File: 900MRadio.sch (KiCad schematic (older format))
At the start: 0 parts

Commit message: Added more RF components
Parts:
- added U3: CC1120, SMD_Packages:RHB_S-PVQFN-N32, symbol CC1120
- added U4: CC1190, SMD_Packages:RGV_S-PVQFN-N16, symbol CC1190
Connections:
- new net GND: U3.EP (GND), U4.1 (GND), U4.12 (GND), U4.3 (GND), U4.9 (GND), U4.EP (GND)
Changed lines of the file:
@@
 $Descr A4 11693 8268
 encoding utf-8
-Sheet 1 3
+Sheet 3 3
 Title ""
 Date ""
@@
 Comment4 ""
 $EndDescr
+$Comp
+L CC1120 U3
+U 1 1 559BFDEE
+P 2900 3850
+F 0 "U3" H 2400 2800 60  0000 C CNN
+F 1 "CC1120" H 3250 2800 60  0000 C CNN
+F 2 "SMD_Packages:RHB_S-PVQFN-N32" H 2900 3850 60  0001 C CNN
+F 3 "" H 2900 3850 60  0000 C CNN
+	1    2900 3850
+	1    0    0    -1
+$EndComp
+$Comp
+L GND #PWR021
+U 1 1 559BFF7D
+P 2900 5000
+F 0 "#PWR021" H 2900 4750 50  0001 C CNN
+F 1 "GND" H 2900 4850 50  0000 C CNN
+F 2 "" H 2900 5000 60  0000 C CNN
+F 3 "" H 2900 5000 60  0000 C CNN
+	1    2900 5000
+	1    0    0    -1
+$EndComp
+$Comp
+L CC1190 U4
+U 1 1 559C0282
+P 7050 4250
+F 0 "U4" H 6600 3700 60  0000 C CNN
+F 1 "CC1190" H 6700 4800 60  0000 C CNN
+F 2 "SMD_Packages:RGV_S-PVQFN-N16" H 7050 4250 60  0001 C CNN
+F 3 "" H 7050 4250 60  0000 C CNN
+	1    7050 4250
+	1    0    0    -1
+$EndComp
+$Comp
+L GND #PWR022
+U 1 1 559C0581
+P 7050 4900
+F 0 "#PWR022" H 7050 4650 50  0001 C CNN
+F 1 "GND" H 7050 4750 50  0000 C CNN
+F 2 "" H 7050 4900 60  0000 C CNN
+F 3 "" H 7050 4900 60  0000 C CNN
+	1    7050 4900
+	1    0    0    -1
+$EndComp
 $EndSCHEMATC

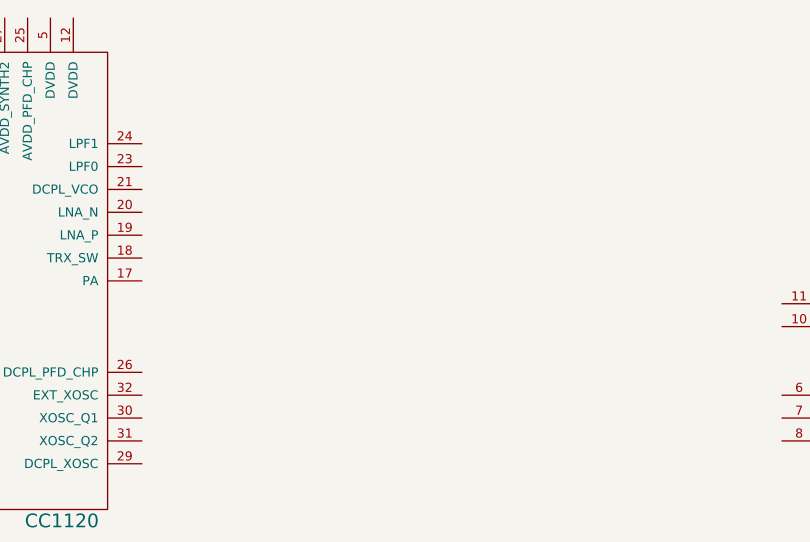
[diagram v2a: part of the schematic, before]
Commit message: Added baluns
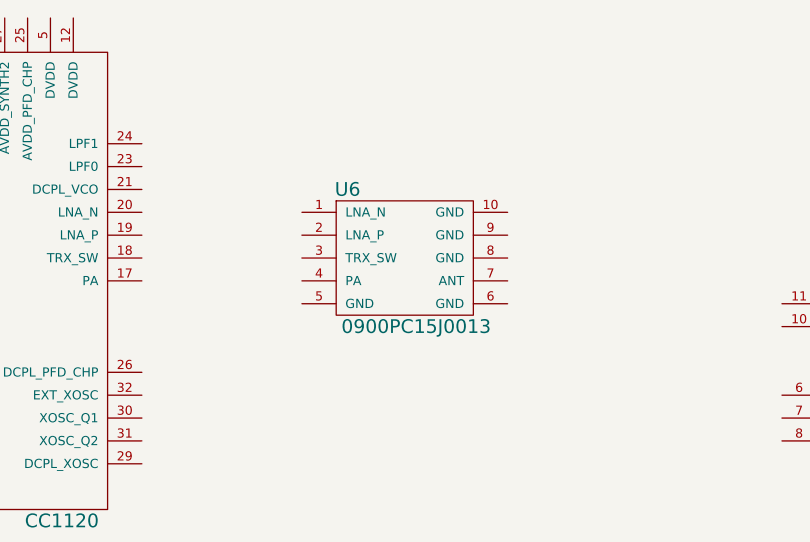
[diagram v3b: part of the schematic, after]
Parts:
- added U6: 0900PC15J0013, SMD_Packages:0900PC15J0013, symbol 0900PC15J0013
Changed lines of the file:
@@
+	1    0    0    -1
+$EndComp
+$Comp
+L 0900PC15J0013 U6
+U 1 1 559C9B74
+P 4750 3750
+F 0 "U6" H 4500 4050 60  0000 C CNN
+F 1 "0900PC15J0013" H 4800 3450 60  0000 C CNN
+F 2 "SMD_Packages:0900PC15J0013" H 4750 3750 60  0001 C CNN
+F 3 "" H 4750 3750 60  0000 C CNN
+	1    4750 3750
 	1    0    0    -1
 $EndComp

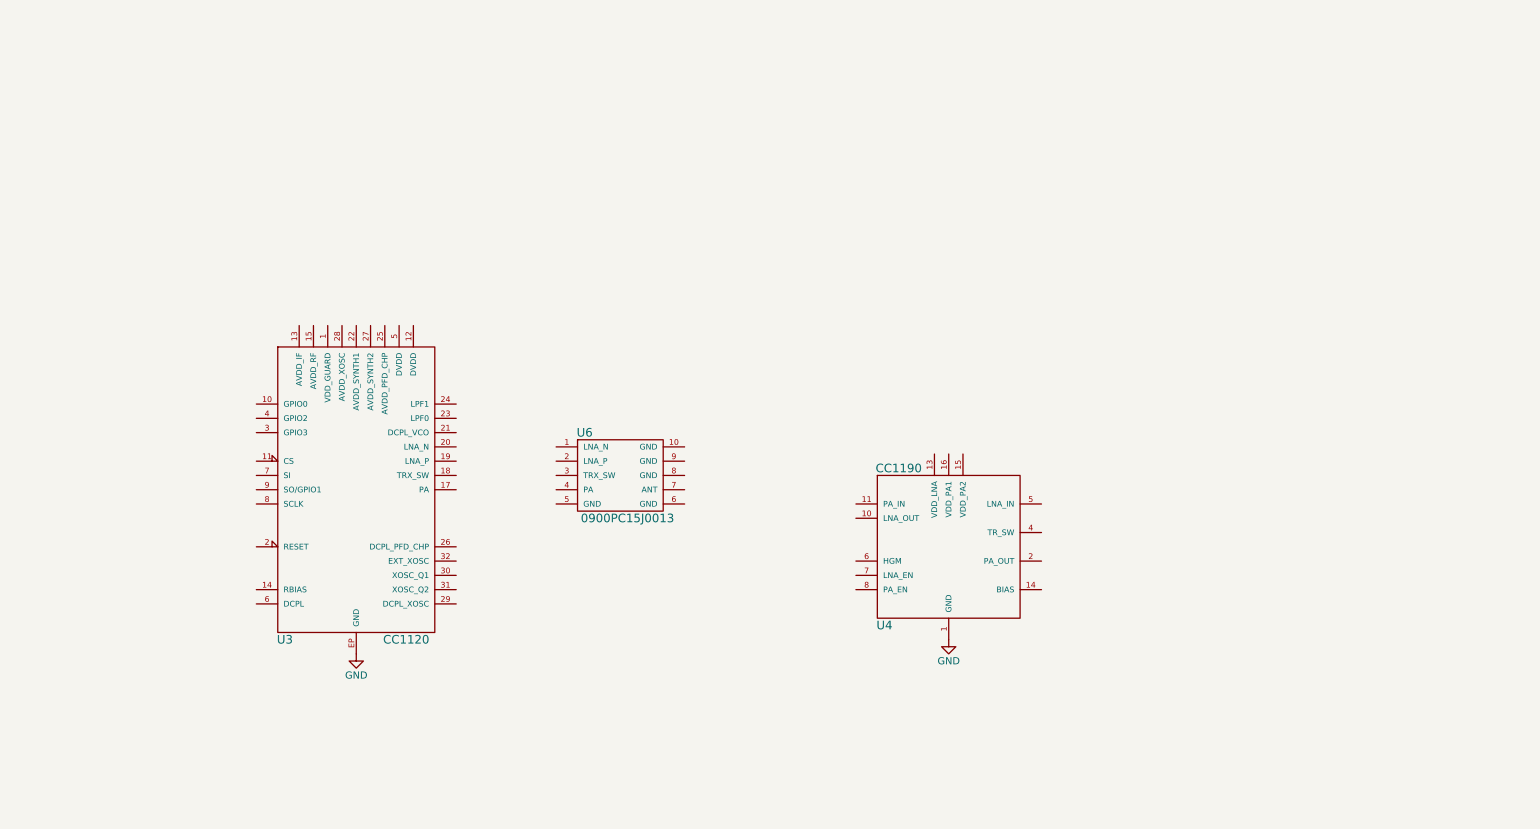
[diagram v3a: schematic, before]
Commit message: Finished schematic of 2.4GHz and 900MHz radios
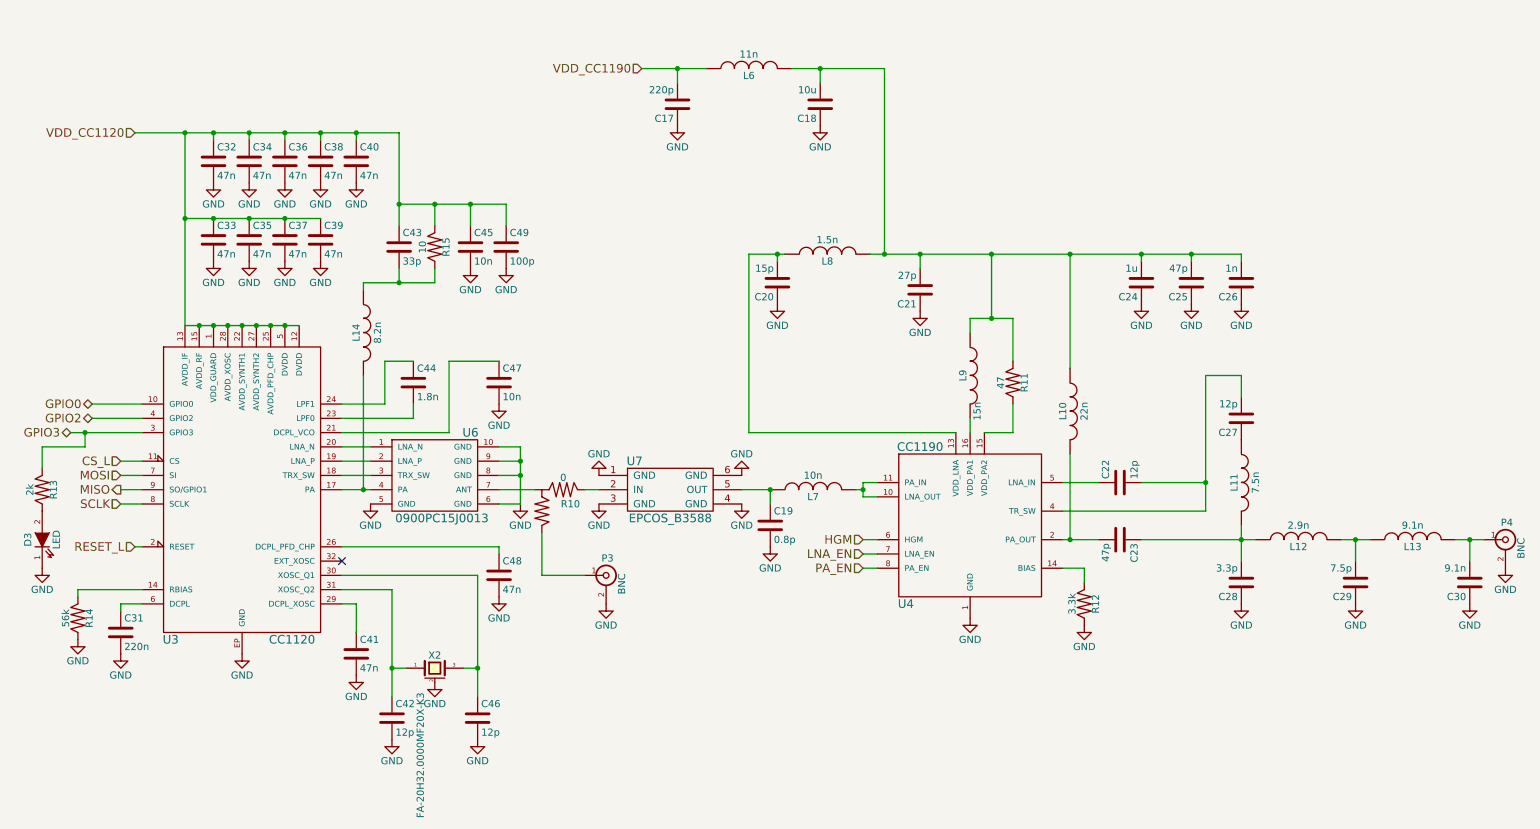
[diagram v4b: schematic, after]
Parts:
- added C17: 220p, Capacitors_SMD:C_0402, symbol C
- added C18: 10u, Capacitors_SMD:C_0402, symbol C
- added C19: 0.8p, Capacitors_SMD:C_0402, symbol C
- added C20: 15p, Capacitors_SMD:C_0402, symbol C
- added C21: 27p, Capacitors_SMD:C_0402, symbol C
- added C22, C27, C42, C46: 12p, Capacitors_SMD:C_0402, symbol C
- added C23, C25: 47p, Capacitors_SMD:C_0402, symbol C
- added C24: 1u, Capacitors_SMD:C_0402, symbol C
- added C26: 1n, Capacitors_SMD:C_0402, symbol C
- added C28: 3.3p, Capacitors_SMD:C_0402, symbol C
- added C29: 7.5p, Capacitors_SMD:C_0402, symbol C
- added C30: 9.1n, Capacitors_SMD:C_0402, symbol C
- added C31: 220n, Capacitors_SMD:C_0402, symbol C
- added C32, C33, C34, C35, C36, C37, C38, C39, C40, C41, C48: 47n, Capacitors_SMD:C_0402, symbol C
- added C43: 33p, Capacitors_SMD:C_0402, symbol C
- added C44: 1.8n, Capacitors_SMD:C_0402, symbol C
- added C45, C47: 10n, Capacitors_SMD:C_0402, symbol C
- added C49: 100p, Capacitors_SMD:C_0402, symbol C
- added D3: LED, LEDs:LED-0603, symbol LED
- added L10: 22n, Resistors_SMD:R_0402, symbol INDUCTOR
- added L11: 7.5n, Resistors_SMD:R_0402, symbol INDUCTOR
- added L12: 2.9n, Resistors_SMD:R_0402, symbol INDUCTOR
- added L13: 9.1n, Resistors_SMD:R_0402, symbol INDUCTOR
- added L14: 8.2n, Resistors_SMD:R_0402, symbol INDUCTOR
- added L6: 11n, Resistors_SMD:R_0402, symbol INDUCTOR
- added L7: 10n, Resistors_SMD:R_0402, symbol INDUCTOR
- added L8: 1.5n, Resistors_SMD:R_0402, symbol INDUCTOR
- added L9: 15n, Resistors_SMD:R_0402, symbol INDUCTOR
- added P3, P4: BNC, Connect:SMB_Straight, symbol BNC
- added R10: 0, Resistors_SMD:R3_LH_0402, symbol R3-LH
- added R11: 47, Resistors_SMD:R_0402, symbol R
- added R12: 3.3k, Resistors_SMD:R_0402, symbol R
- added R13: 2k, Resistors_SMD:R_0402, symbol R
- added R14: 56k, Resistors_SMD:R_0402, symbol R
- added R15: 10, Resistors_SMD:R_0402, symbol R
- added U7: EPCOS_B3588, SMD_Packages:DCC6C, symbol EPCOS_B3588
- added X2: FA-20H32.0000MF20X-K3, Crystals_Oscillators_SMD:FA-20H, symbol CRYSTAL_SMD
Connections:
- net GND: now also U6.10 (GND), U6.5 (GND), U6.6 (GND), U6.8 (GND), U6.9 (GND), C17.1, C18.1, C19.2, C20.1, C21.1, C24.1, C25.1, C26.1, C28.1, C29.1, C30.1, C31.2, C32.2, C33.2, C34.2, C35.2, C36.2, C37.2, C38.2, C39.2, C40.2, C41.2, C42.2, C45.2, C46.2, C47.2, C48.2, C49.2, D3.1 (K), P3.2 (Ext), P4.2 (Ext), R12.2, R14.2, U7.1 (GND), U7.3 (GND), U7.4 (GND), U7.6 (GND), X2.2 (gnd), X2.4 (gnd)
- net VDD_CC1120: now reaches U3.1 (VDD_GUARD)
- net VDD_CC1120: now also U3.12 (DVDD), U3.13 (AVDD_IF), U3.15 (AVDD_RF), U3.22 (AVDD_SYNTH1), U3.25 (AVDD_PFD_CHP), U3.27 (AVDD_SYNTH2), U3.28 (AVDD_XOSC), U3.5 (DVDD), C32.1, C33.1, C34.1, C35.1, C36.1, C37.1, C38.1, C39.1, C40.1, C43.1, C45.1, C49.1, R15.1
- net GPIO0: now reaches U3.10 (GPIO0)
- net CS_L: now reaches U3.11 (CS)
- net at U3.14 (RBIAS): now also R14.1
- net at U3.17 (PA): now also U6.4 (PA), L14.2
- net at U3.18 (TRX_SW): now also U6.3 (TRX_SW)
- net at U3.19 (LNA_P): now also U6.2 (LNA_P)
- net RESET_L: now reaches U3.2 (RESET)
- net at U3.20 (LNA_N): now also U6.1 (LNA_N)
- net at U3.21 (DCPL_VCO): now also C47.1
- net at U3.23 (LPF0): now also C44.2
- net at U3.24 (LPF1): now also C44.1
- net at U3.26 (DCPL_PFD_CHP): now also C48.1
- net at U3.29 (DCPL_XOSC): now also C41.1
- net GPIO3: now reaches U3.3 (GPIO3)
- net GPIO3: now also R13.1
- net at U3.30 (XOSC_Q1): now also C46.1, X2.3
- net at U3.31 (XOSC_Q2): now also C42.1, X2.1
- net GPIO2: now reaches U3.4 (GPIO2)
- net at U3.6 (DCPL): now also C31.1
- net MOSI: now reaches U3.7 (SI)
- net SCLK: now reaches U3.8 (SCLK)
- net MISO: now reaches U3.9 (SO/GPIO1)
- net at U4.10 (LNA_OUT): now also U4.11 (PA_IN), L7.2
- net at U4.13 (VDD_LNA): now also C20.2, L8.1
- net at U4.14 (BIAS): now also R12.1
- net at U4.15 (VDD_PA2): now also R11.2
- net at U4.16 (VDD_PA1): now also L9.2
- net at U4.2 (PA_OUT): now also C23.2, L10.2
- net at U4.4 (TR_SW): now also C22.2, C27.2
- net at U4.5 (LNA_IN): now also C22.1
- net HGM: now reaches U4.6 (HGM)
- net LNA_EN: now reaches U4.7 (LNA_EN)
- net PA_EN: now reaches U4.8 (PA_EN)
- net at U6.7 (ANT): now also R10.2
- new net: C30.2, L13.2, P4.1 (In)
- new net: P3.1 (In), R10.3
- new net: R10.1, U7.2 (IN)
- new net: C19.1, L7.1, U7.5 (OUT)
- new net: C23.1, C28.2, L11.2, L12.1
- new net: C18.2, C21.2, C24.2, C25.2, C26.2, L10.1, L6.2, L8.2, L9.1, R11.1
- new net: C29.2, L12.2, L13.1
- new net: C27.1, L11.1
- new net: D3.2 (A), R13.2
- new net: C43.2, L14.1, R15.2
- new net VDD_CC1190: C17.2, L6.1
- no-connect marks 0 -> 1
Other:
- moved on the sheet: U3, U4, U6

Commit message: Updated layout
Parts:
- added C50: 100n, Capacitors_SMD:C_0402, symbol C
- added C51: 2u2, Capacitors_SMD:C_0402, symbol C
- added L15: FERRITE BEAD, Resistors_SMD:R_0402, symbol INDUCTOR
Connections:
- net GND: now also C50.2, C51.2
- net VDD_CC1120: now also C50.1, L15.1; no longer C32.1, C33.1, C34.1, C35.1, C36.1, C37.1, C38.1, C39.1, C40.1, C43.1, C45.1, C49.1, R15.1, U3.1 (VDD_GUARD), U3.12 (DVDD), U3.13 (AVDD_IF), U3.15 (AVDD_RF), U3.22 (AVDD_SYNTH1), U3.25 (AVDD_PFD_CHP), U3.27 (AVDD_SYNTH2), U3.28 (AVDD_XOSC), U3.5 (DVDD)
- net CC11990_VDD_ISO: now reaches C18.2, C21.2, C24.2, C25.2, C26.2, L10.1, L6.2, L8.2, L9.1, R11.1
- new net VDD_CC1120_ISO: C32.1, C33.1, C34.1, C35.1, C36.1, C37.1, C38.1, C39.1, C40.1, C43.1, C45.1, C49.1, C51.1, L15.2, R15.1, U3.1 (VDD_GUARD), U3.12 (DVDD), U3.13 (AVDD_IF), U3.15 (AVDD_RF), U3.22 (AVDD_SYNTH1), U3.25 (AVDD_PFD_CHP), U3.27 (AVDD_SYNTH2), U3.28 (AVDD_XOSC), U3.5 (DVDD)
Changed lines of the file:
@@
 	1    0    0    -1
 $EndComp
-Text HLabel 1350 1350 0    60   Input ~ 0
+Text HLabel 1200 650  0    60   Input ~ 0
 VDD_CC1120
 $Comp
@@
 	3950 1850 3950 2000
 Connection ~ 3700 1850
-Wire Wire Line
-	1350 1350 3200 1350
 Connection ~ 3200 1850
 Wire Wire Line
@@
 	3450 2400 3450 2300
 Wire Wire Line
-	2650 1400 2650 1350
+	2650 650  2650 1400
 Connection ~ 2650 1350
 Wire Wire Line
-	2900 1400 2900 1350
+	2900 1350 2900 1400
 Connection ~ 2900 1350
 Wire Wire Line
@@
 Connection ~ 1900 1350
 Wire Wire Line
-	2150 1400 2150 1350
+	2150 1350 2150 1400
 Connection ~ 2150 1350
 Wire Wire Line
-	2400 1400 2400 1350
+	2400 1350 2400 1400
 Connection ~ 2400 1350
 $Comp
@@
 	1    0    0    -1
 $EndComp
+Text Label 7050 2200 0    60   ~ 0
+CC11990_VDD_ISO
+Wire Wire Line
+	1700 1350 3200 1350
+$Comp
+L C C50
+U 1 1 55A3DD63
+P 1300 800
+F 0 "C50" H 1325 900 50  0000 L CNN
+F 1 "100n" H 1325 700 50  0000 L CNN
+F 2 "Capacitors_SMD:C_0402" H 1338 650 30  0001 C CNN
+F 3 "" H 1300 800 60  0000 C CNN
+	1    1300 800
+	1    0    0    -1
+$EndComp
+$Comp
+L GND #PWR068
+U 1 1 55A3DEF6
+P 1300 950
+F 0 "#PWR068" H 1300 700 50  0001 C CNN
+F 1 "GND" H 1300 800 50  0000 C CNN
+F 2 "" H 1300 950 60  0000 C CNN
+F 3 "" H 1300 950 60  0000 C CNN
+	1    1300 950
+	1    0    0    -1
+$EndComp
+$Comp
+L C C51
+U 1 1 55A3E090
+P 2200 800
+F 0 "C51" H 2225 900 50  0000 L CNN
+F 1 "2u2" H 2225 700 50  0000 L CNN
+F 2 "Capacitors_SMD:C_0402" H 2238 650 30  0001 C CNN
+F 3 "" H 2200 800 60  0000 C CNN
+	1    2200 800
+	1    0    0    -1
+$EndComp
+$Comp
+L GND #PWR069
+U 1 1 55A3E2B7
+P 2200 950
+F 0 "#PWR069" H 2200 700 50  0001 C CNN
+F 1 "GND" H 2200 800 50  0000 C CNN
+F 2 "" H 2200 950 60  0000 C CNN
+F 3 "" H 2200 950 60  0000 C CNN
+	1    2200 950
+	1    0    0    -1
+$EndComp
+$Comp
+L INDUCTOR L15
+U 1 1 55A3E656
+P 1750 650
+F 0 "L15" V 1700 650 50  0000 C CNN
+F 1 "FERRITE BEAD" V 1850 650 50  0000 C CNN
+F 2 "Resistors_SMD:R_0402" H 1750 650 60  0001 C CNN
+F 3 "" H 1750 650 60  0000 C CNN
+	1    1750 650
+	0    -1   -1   0
+$EndComp
+Wire Wire Line
+	1200 650  1450 650
+Connection ~ 1300 650
+Wire Wire Line
+	2050 650  2650 650
+Connection ~ 2200 650
+Text Label 2650 650  0    60   ~ 0
+VDD_CC1120_ISO
 $EndSCHEMATC

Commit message: Mostly finished up 900MHz routing.
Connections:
- net CC11990_VDD_ISO renamed VDD_CC1190_ISO
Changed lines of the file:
@@
 $EndComp
 Text Label 7050 2200 0    60   ~ 0
-CC11990_VDD_ISO
+VDD_CC1190_ISO
 Wire Wire Line
 	1700 1350 3200 1350
